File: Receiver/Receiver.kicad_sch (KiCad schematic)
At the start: 6 parts, among them U1 NUCLEO64-F401RE, U2 HM-10

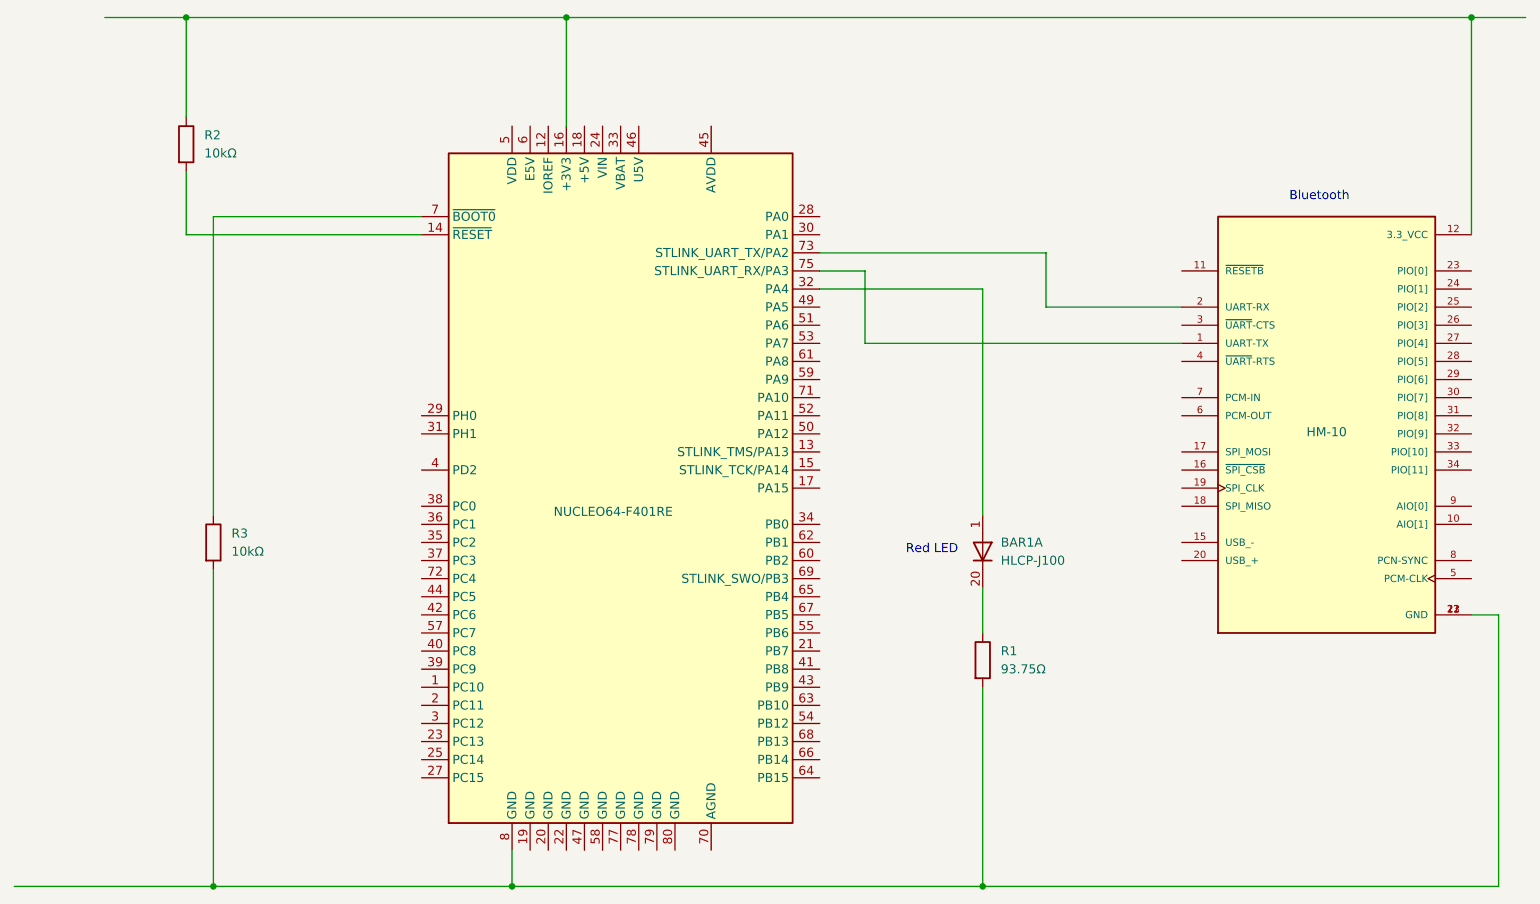
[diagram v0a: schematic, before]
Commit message: Rematch the pins on schematics between HC-05 and STM32
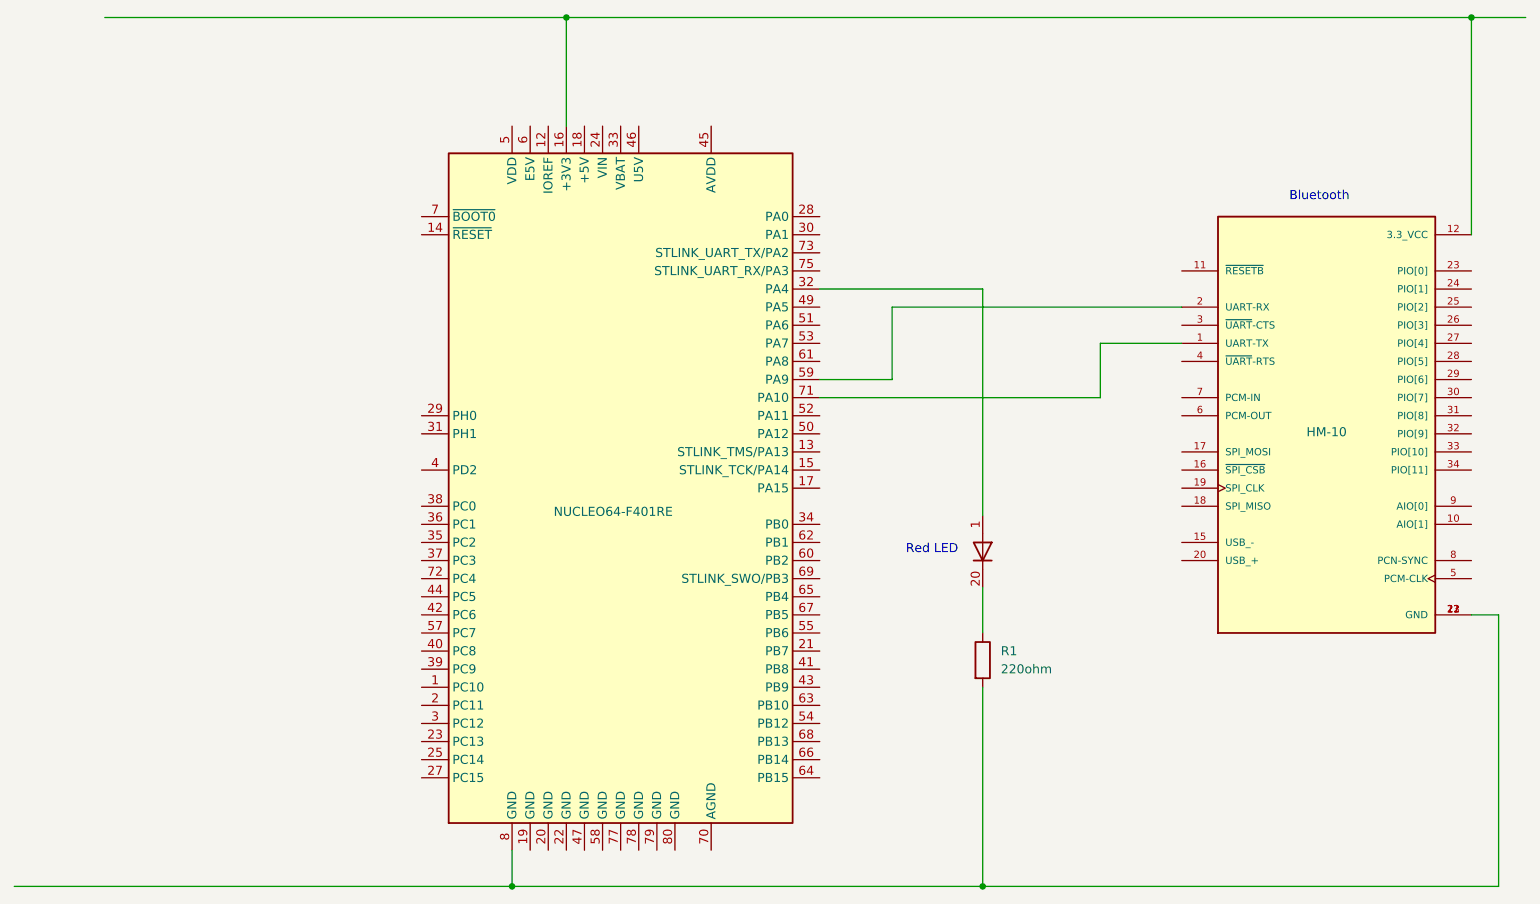
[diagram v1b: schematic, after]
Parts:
- removed R2, R3: 10kΩ, symbol Device:R
- R1: value 93.75Ω -> 220ohm
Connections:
- net at U2.1 (UART-TX): now also U1.71 (PA10); no longer U1.75 (STLINK_UART_RX/PA3)
- net at U2.2 (UART-RX): now also U1.59 (PA9); no longer U1.73 (STLINK_UART_TX/PA2)

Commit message: Add buzzer in schematics of receiver
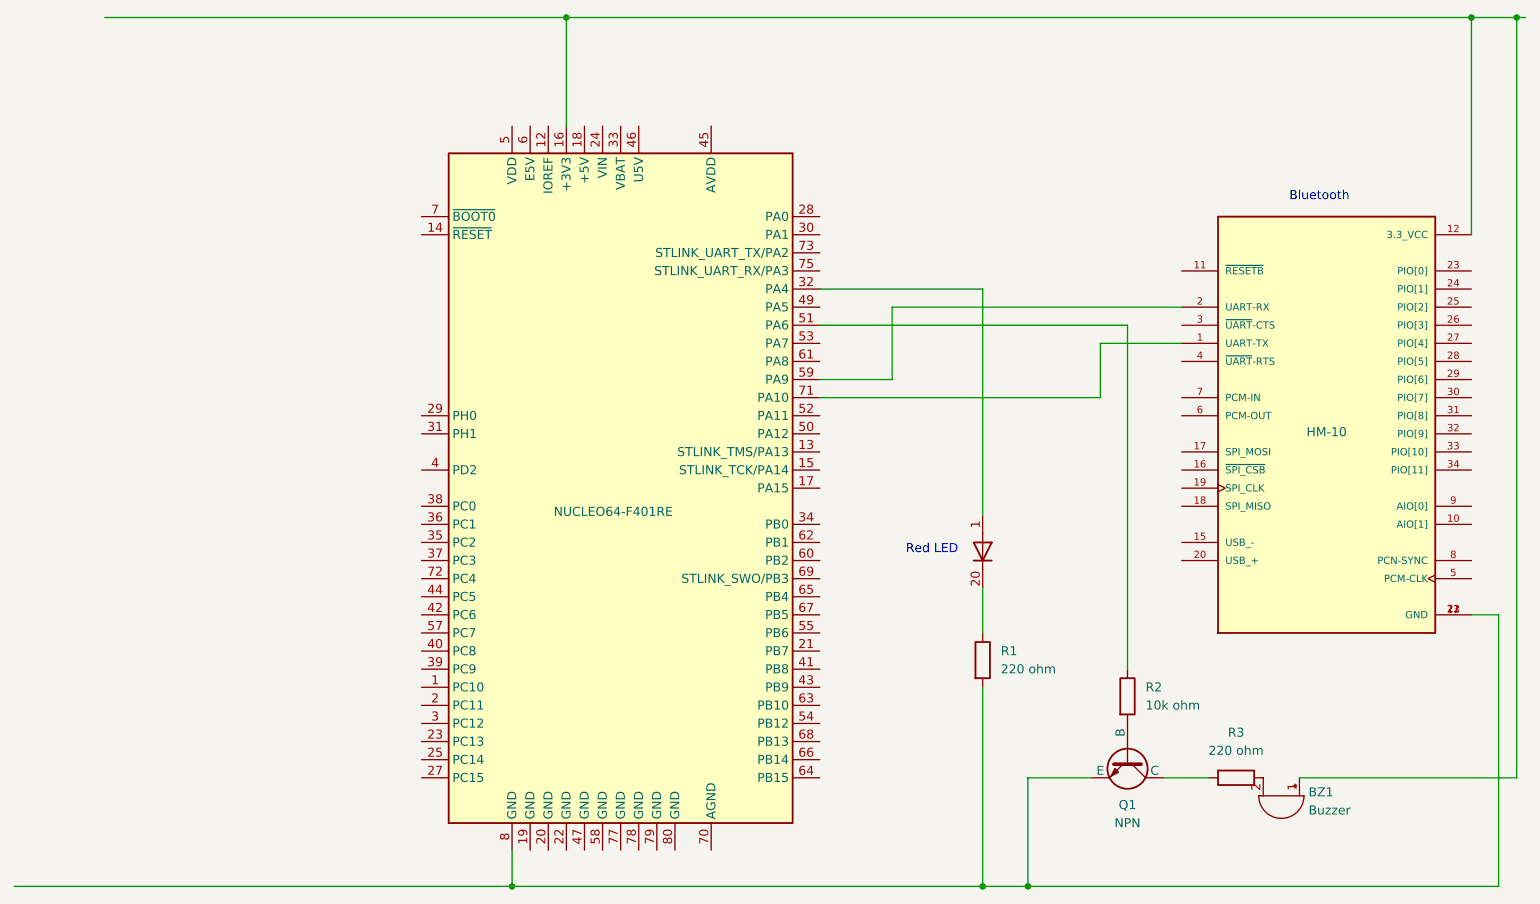
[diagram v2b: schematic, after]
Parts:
- added BZ1: Buzzer, symbol Device:Buzzer
- added Q1: NPN, symbol Simulation_SPICE:NPN
- added R2: 10k ohm, symbol Device:R
- added R3: 220 ohm, symbol Device:R
- R1: value 220ohm -> 220 ohm
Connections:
- net at U1.16 (+3V3), U2.12 (3.3_VCC): now also BZ1.1 (+)
- net at R1.2, U1.8 (GND), U2.13 (GND)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: now also Q1.3 (E)
- net at U1.51 (PA6): now also R2.1
- new net: BZ1.2 (-), R3.1
- new net: Q1.1 (C), R3.2
- new net: Q1.2 (B), R2.2

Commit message: Update the Bluetooth module to be HC-05
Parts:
- U2: value HM-10 -> HC-05
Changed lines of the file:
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@@
 			)
 		)
-		(property "Value" "HM-10"
+		(property "Value" "HC-05"
 			(at 213.36 88.646 0)
 			(effects

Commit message: Update Voltage supply to be 5 volts
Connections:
- net at BZ1.1 (+), U2.12 (3.3_VCC): now also U1.18 (+5V); no longer U1.16 (+3V3)
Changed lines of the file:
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@@
 	)
 	(junction
-		(at 106.68 30.48)
+		(at 110.49 30.48)
 		(diameter 0)
 		(color 0 0 0 0)
@@
 	(wire
 		(pts
+			(xy 110.49 30.48) (xy 233.68 30.48)
+		)
+		(stroke
+			(width 0)
+			(type default)
+			(color 255 0 0 1)
+		)
+	)
+	(wire
+		(pts
 			(xy 165.1 124.46) (xy 165.1 152.4)
 		)
@@
 	(wire
 		(pts
+			(xy 110.49 30.48) (xy 110.49 45.72)
+		)
+		(stroke
+			(width 0)
+			(type default)
+			(color 255 0 0 1)
+		)
+	)
+	(wire
+		(pts
 			(xy 193.04 71.12) (xy 152.4 71.12)
 		)
@@
 	(wire
 		(pts
+			(xy 110.49 45.72) (xy 109.22 45.72)
+		)
+		(stroke
+			(width 0)
+			(type default)
+			(color 255 0 0 1)
+		)
+	)
+	(wire
+		(pts
 			(xy 181.61 83.82) (xy 181.61 76.2)
 		)
@@
 	(wire
 		(pts
-			(xy 106.68 30.48) (xy 233.68 30.48)
+			(xy 41.91 30.48) (xy 110.49 30.48)
 		)
 		(stroke
@@
 		)
 	)
-	(wire
-		(pts
-			(xy 41.91 30.48) (xy 106.68 30.48)
-		)
-		(stroke
-			(width 0)
-			(type default)
-			(color 255 0 0 1)
-		)
-	)
-	(wire
-		(pts
-			(xy 106.68 30.48) (xy 106.68 45.72)
-		)
-		(stroke
-			(width 0)
-			(type default)
-			(color 255 0 0 1)
-		)
-	)
